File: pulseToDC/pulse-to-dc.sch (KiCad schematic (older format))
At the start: 13 parts

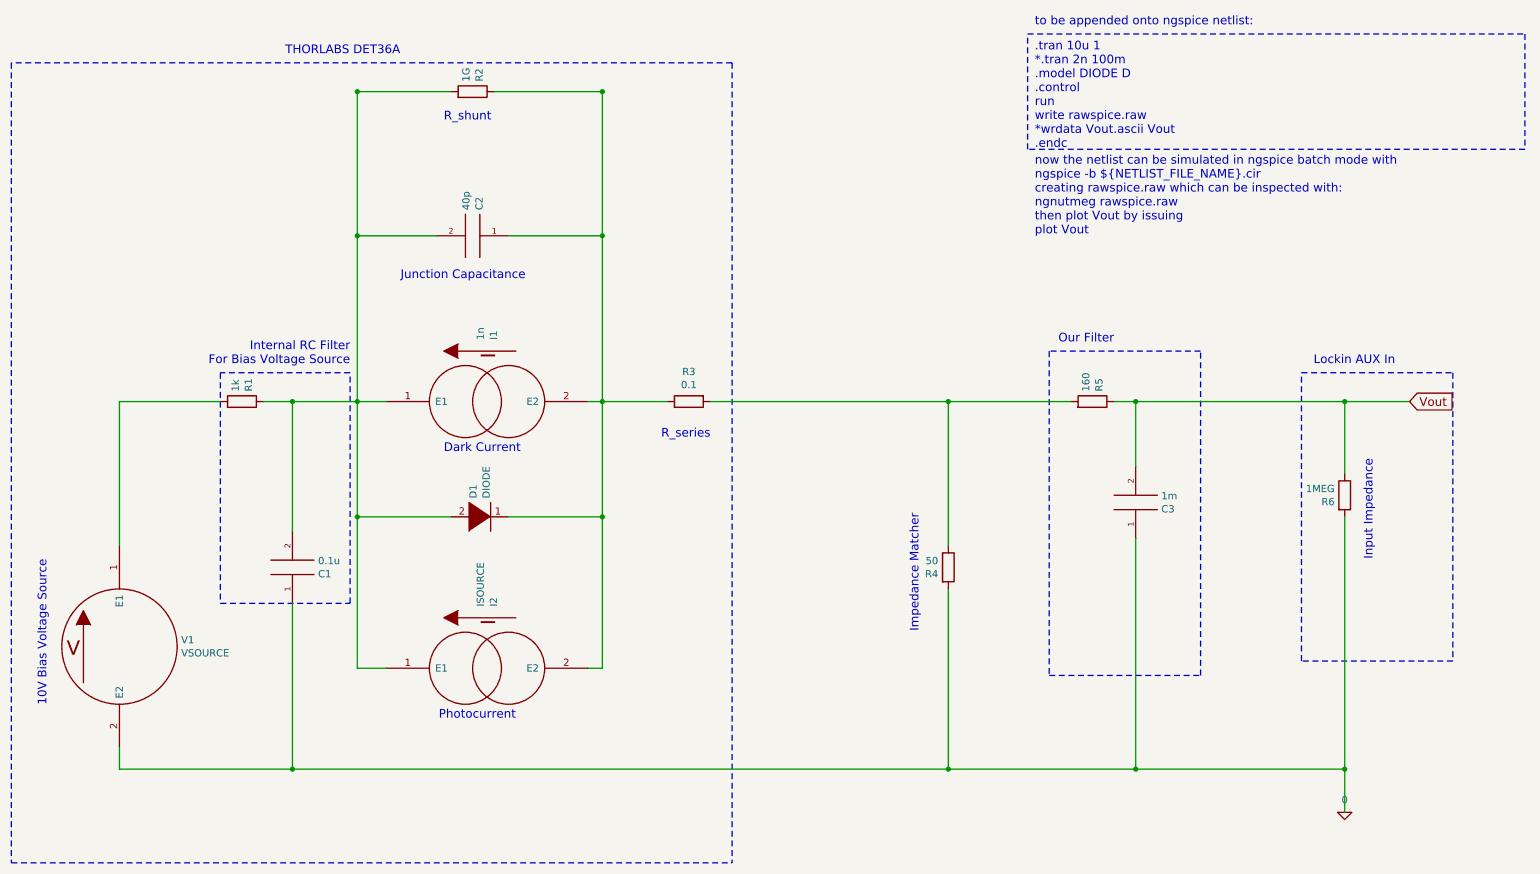
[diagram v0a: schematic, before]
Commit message: new filter setup
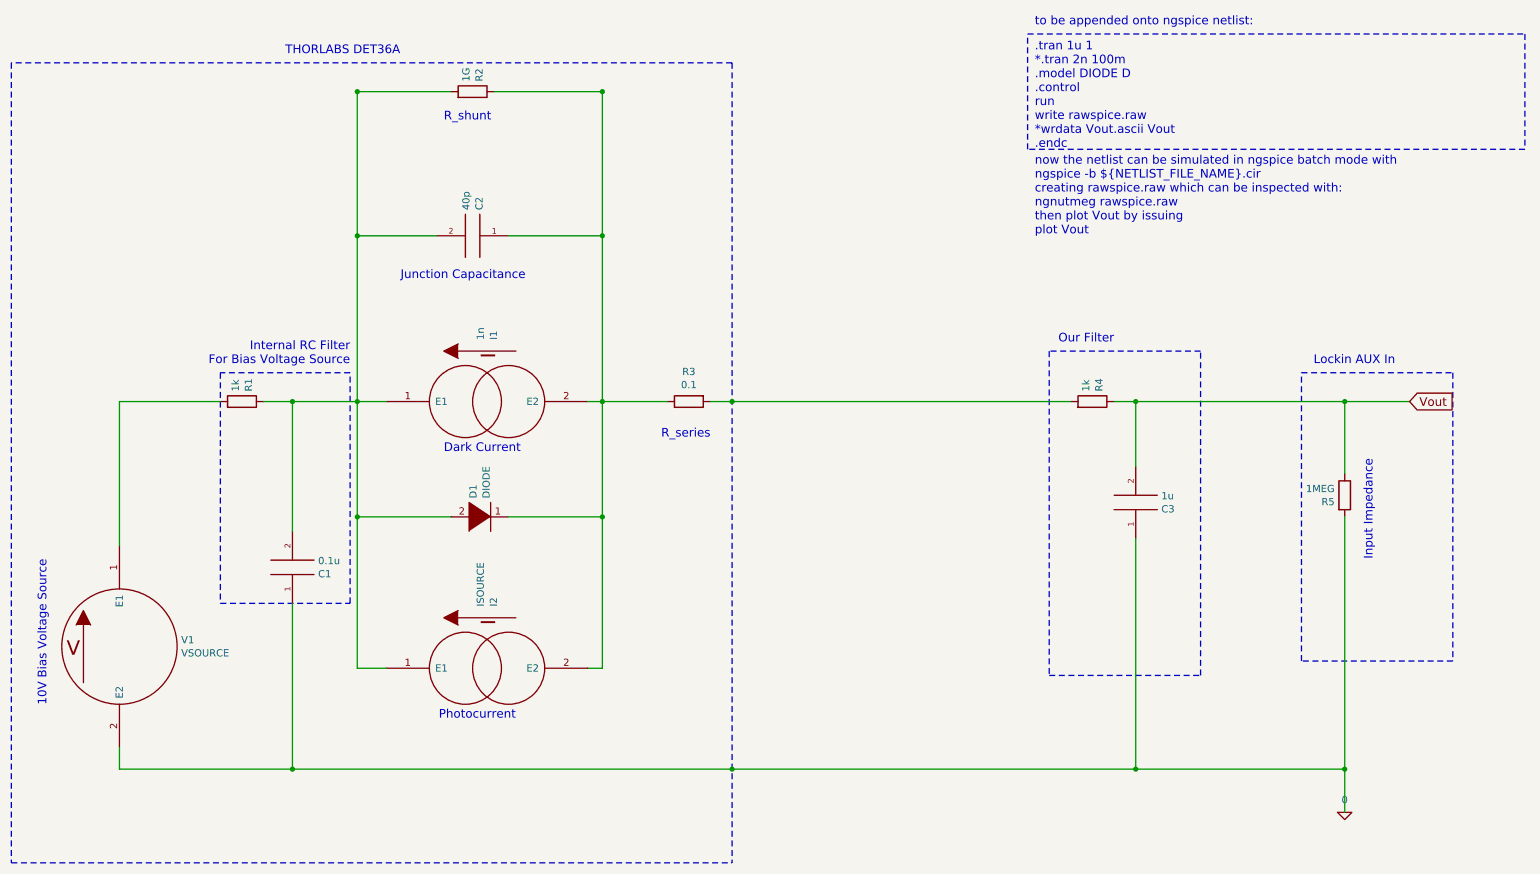
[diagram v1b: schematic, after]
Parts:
- removed R5: 160, symbol R
- C3: value 1m -> 1u
- R4: value 50 -> 1k
- renumbered R6 to R5
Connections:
- net 0: no longer R4.2
- net Vout: now also R4.1
- net at R3.2: now also R4.2; no longer R4.1
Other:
- note added: ".tran 1u 1\n*.tran 2n 100m\n.model DIODE D\n.control\nrun\nwrite rawspice.raw\n*wrdata Vout.ascii Vout\n.endc"
- note removed: ".tran 10u 1\n*.tran 2n 100m\n.model DIODE D\n.control\nrun\nwrite rawspice.raw\n*wrdata Vout.ascii Vout\n.endc"
- note removed: "Impedance Matcher"
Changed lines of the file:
@@
 Our Filter
 Text Notes 7600 1550 0    60   ~ 0
-.tran 10u 1\n*.tran 2n 100m\n.model DIODE D\n.control\nrun\nwrite rawspice.raw\n*wrdata Vout.ascii Vout\n.endc
+.tran 1u 1\n*.tran 2n 100m\n.model DIODE D\n.control\nrun\nwrite rawspice.raw\n*wrdata Vout.ascii Vout\n.endc
 Text Notes 7600 700  0    60   ~ 0
 to be appended onto ngspice netlist:
 Text Notes 7600 2150 0    60   ~ 0
 now the netlist can be simulated in ngspice batch mode with\nngspice -b ${NETLIST_FILE_NAME}.cir\ncreating rawspice.raw which can be inspected with:\nngnutmeg rawspice.raw\nthen plot Vout by issuing\nplot Vout
-$Comp
-L R R4
-U 1 1 594A3F57
-P 7000 4450
-F 0 "R4" H 6930 4404 50  0000 R CNN
-F 1 "50" H 6930 4495 50  0000 R CNN
-F 2 "" V 6930 4450 50  0001 C CNN
-F 3 "" H 7000 4450 50  0001 C CNN
-	1    7000 4450
-	1    0    0    -1
-$EndComp
-Text Notes 6800 4900 1    60   ~ 0
-Impedance Matcher
 Text Notes 9950 4400 1    60   ~ 0
 Input Impedance
@@
 10V Bias Voltage Source
 $Comp
-L R R6
+L R R5
 U 1 1 594A9D92
 P 9750 3950
-F 0 "R6" H 9680 3904 50  0000 R CNN
+F 0 "R5" H 9680 3904 50  0000 R CNN
 F 1 "1MEG" H 9680 3995 50  0000 R CNN
 F 2 "" V 9680 3950 50  0001 C CNN
@@
 	1    9750 3950
 	1    0    0    -1
-$EndComp
-$Comp
-L CAP C3
-U 1 1 594AA48B
-P 8300 4000
-F 0 "C3" H 8478 4046 50  0000 L CNN
-F 1 "1m" H 8478 3955 50  0000 L CNN
-F 2 "" H 8300 4000 50  0001 C CNN
-F 3 "" H 8300 4000 50  0001 C CNN
-	1    8300 4000
-	1    0    0    1
 $EndComp
 Wire Wire Line
@@
 	1250 5850 9750 5850
 Connection ~ 9750 5850
-Wire Wire Line
-	5350 3300 7850 3300
-Wire Wire Line
-	8150 3300 10200 3300
 $Comp
-L R R5
-U 1 1 594AA3CF
+L CAP C3
+U 1 1 594C0352
+P 8300 4000
+F 0 "C3" H 8478 4046 50  0000 L CNN
+F 1 "1u" H 8478 3955 50  0000 L CNN
+F 2 "" H 8300 4000 50  0001 C CNN
+F 3 "" H 8300 4000 50  0001 C CNN
+	1    8300 4000
+	1    0    0    1
+$EndComp
+$Comp
+L R R4
+U 1 1 594C03EC
 P 8000 3300
-F 0 "R5" H 8070 3346 50  0000 L CNN
-F 1 "160" H 8070 3255 50  0000 L CNN
+F 0 "R4" H 8070 3346 50  0000 L CNN
+F 1 "1k" H 8070 3255 50  0000 L CNN
 F 2 "" V 7930 3300 50  0001 C CNN
 F 3 "" H 8000 3300 50  0001 C CNN
@@
 $EndComp
 Wire Wire Line
-	7000 4300 7000 3300
-Connection ~ 7000 3300
+	5350 3300 7850 3300
 Wire Wire Line
-	7000 4600 7000 5850
-Connection ~ 7000 5850
+	8150 3300 10200 3300
+Connection ~ 5500 5850
+Connection ~ 5500 3300
 $EndSCHEMATC
